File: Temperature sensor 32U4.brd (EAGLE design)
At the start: 66 x 35.6 mm, 30 parts, among them IC1 ATMEGA32U4-AU, IC2 LM2940CS-5.0_NOPB, T1 BD139, X1 16MHz

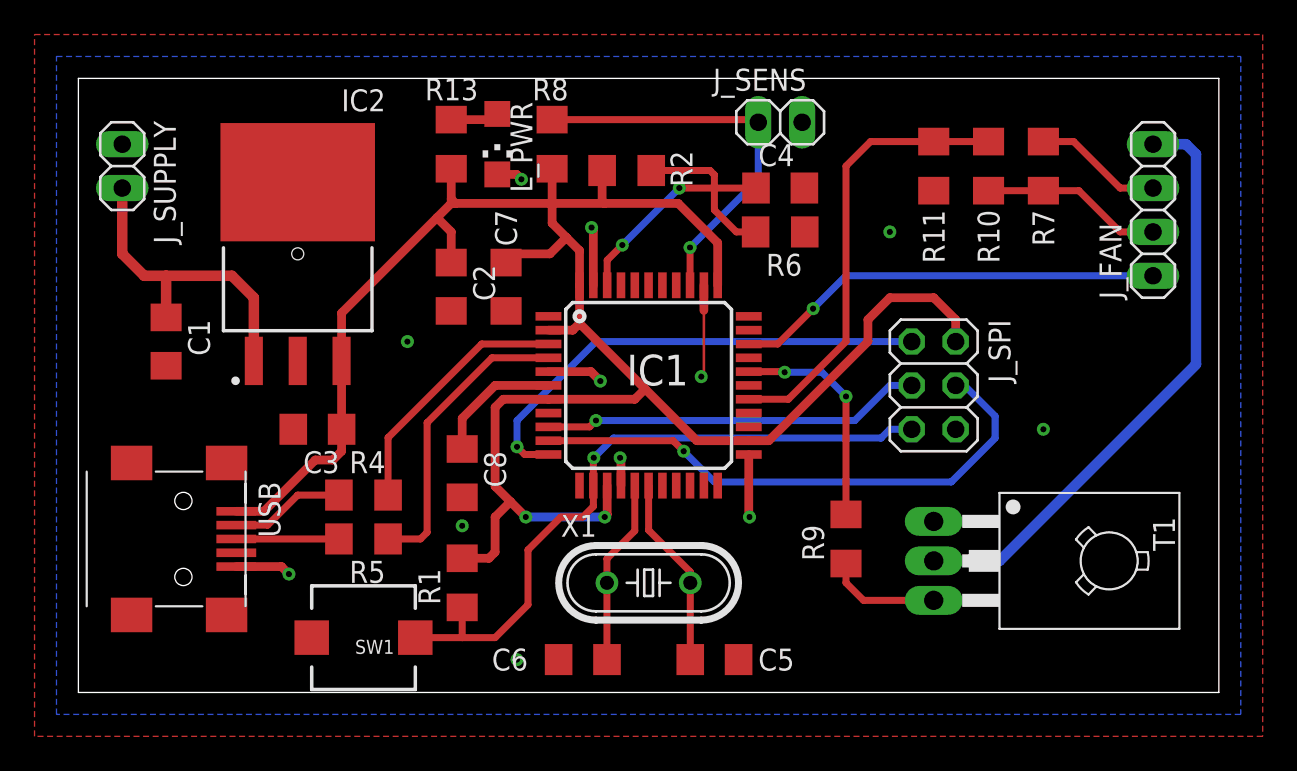
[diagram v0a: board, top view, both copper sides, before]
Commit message: Fixed schematic and deleted backup files
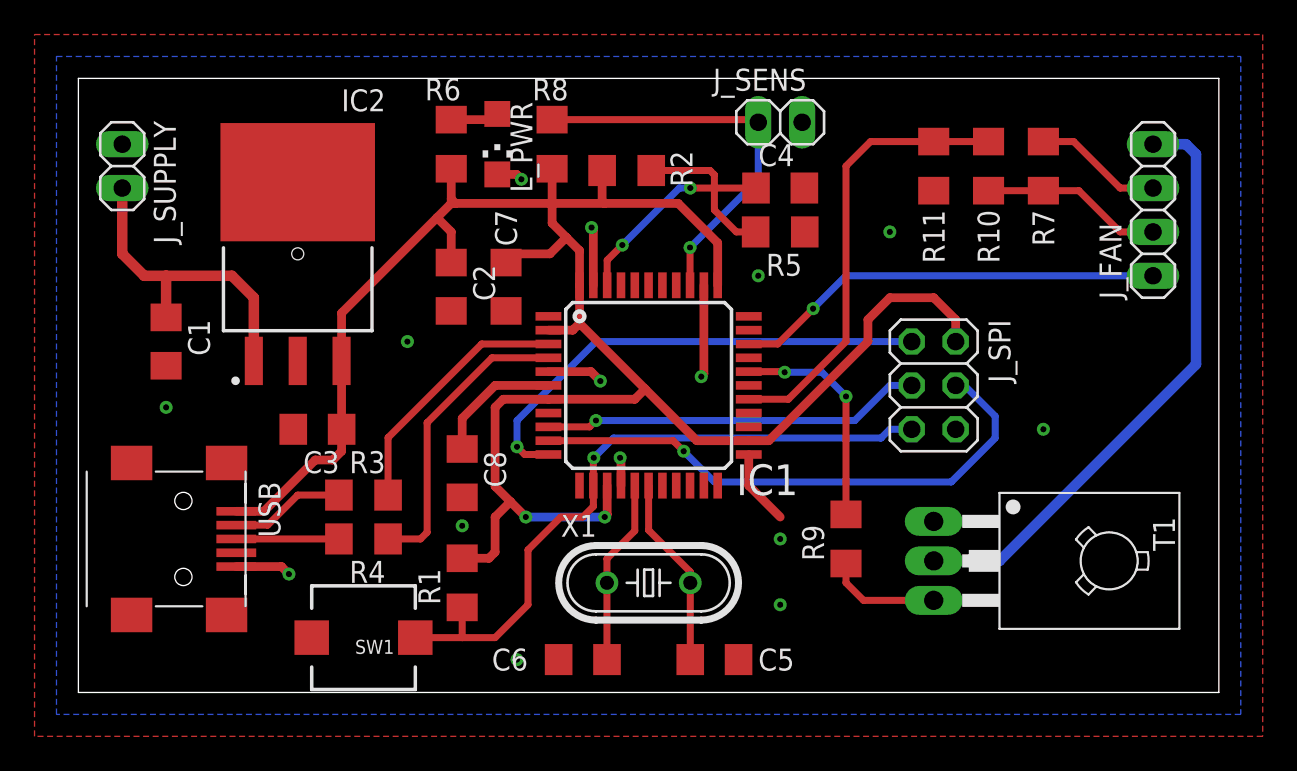
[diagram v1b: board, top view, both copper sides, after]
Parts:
- removed R13: 270, rcl:R1206
- added R3: 10, rcl:R1206
- R5: value 10 -> 8,2k
- R6: value 8,2k -> 270
- moved R5 30.0 mm to (40.6, 26.7)
- moved R6 19.7 mm to (21.6, 31.8), turned to 90 degrees
- moved R4 2.54 mm to (16.5, 8.89)
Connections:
- net +5V: now also R6.1; no longer R13.1
- net AREF: now also R5.2; no longer R6.2
- net D+: now also R4.1; no longer R5.1
- net D-: now also R3.1; no longer R4.1
- net GND: now also R5.1; no longer R6.1
- net N$1: now also R6.2; no longer R13.2
- net USB_D+: now also R4.2; no longer R5.2
- net USB_D-: now also R3.2; no longer R4.2
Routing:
- net GND: track 23.4 -> 22.7 mm, vias 12 -> 15
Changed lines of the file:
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@@
 </element>
 <element name="IC1" library="adafruit" package="TQFP44" value="ATMEGA32U4-AU" x="33.02" y="17.78" smashed="yes">
-<attribute name="NAME" x="31.749996875" y="17.779996875" size="1.778" layer="25"/>
+<attribute name="NAME" x="38.1" y="11.43" size="1.778" layer="25"/>
 </element>
 <element name="IC2" library="LM2940CS-5.0_NOPB" package="TO254P1435X464-4N" value="LM2940CS-5.0_NOPB" x="12.7" y="25.4" smashed="yes" rot="R90">
@@
 <attribute name="SPICEPREFIX" value="R" x="2.54" y="-25.4" size="1.778" layer="27" rot="R270" display="off"/>
 </element>
-<element name="R13" library="rcl" library_urn="urn:adsk.eagle:library:334" package="R1206" package3d_urn="urn:adsk.eagle:package:23540/2" value="270" x="21.59" y="31.75" smashed="yes" rot="R90">
+<element name="R6" library="rcl" library_urn="urn:adsk.eagle:library:334" package="R1206" package3d_urn="urn:adsk.eagle:package:23540/2" value="270" x="21.59" y="31.75" smashed="yes" rot="R90">
 <attribute name="NAME" x="20.066" y="34.29" size="1.27" layer="25"/>
 <attribute name="POPULARITY" value="41" x="74.93" y="46.99" size="1.778" layer="27" rot="R90" display="off"/>
@@
 <attribute name="SPICEPREFIX" value="R" x="2.54" y="70.866" size="1.778" layer="27" rot="R180" display="off"/>
 </element>
-<element name="R4" library="rcl" library_urn="urn:adsk.eagle:library:334" package="R1206" package3d_urn="urn:adsk.eagle:package:23540/2" value="10" x="16.51" y="11.43" smashed="yes" rot="R180">
+<element name="R3" library="rcl" library_urn="urn:adsk.eagle:library:334" package="R1206" package3d_urn="urn:adsk.eagle:package:23540/2" value="10" x="16.51" y="11.43" smashed="yes" rot="R180">
 <attribute name="NAME" x="17.78" y="13.97" size="1.27" layer="25" rot="R180"/>
 <attribute name="POPULARITY" value="41" x="-8.89" y="58.42" size="1.778" layer="27" rot="R180" display="off"/>
 <attribute name="SPICEPREFIX" value="R" x="-8.89" y="58.42" size="1.778" layer="27" rot="R180" display="off"/>
 </element>
-<element name="R5" library="rcl" library_urn="urn:adsk.eagle:library:334" package="R1206" package3d_urn="urn:adsk.eagle:package:23540/2" value="10" x="16.51" y="8.89" smashed="yes" rot="R180">
+<element name="R4" library="rcl" library_urn="urn:adsk.eagle:library:334" package="R1206" package3d_urn="urn:adsk.eagle:package:23540/2" value="10" x="16.51" y="8.89" smashed="yes" rot="R180">
 <attribute name="NAME" x="17.78" y="7.62" size="1.27" layer="25" rot="R180"/>
 <attribute name="POPULARITY" value="41" x="-13.97" y="55.88" size="1.778" layer="27" rot="R180" display="off"/>
 <attribute name="SPICEPREFIX" value="R" x="-13.97" y="55.88" size="1.778" layer="27" rot="R180" display="off"/>
 </element>
-<element name="R6" library="rcl" library_urn="urn:adsk.eagle:library:334" package="R1206" package3d_urn="urn:adsk.eagle:package:23540/2" value="8,2k" x="40.64" y="26.67" smashed="yes" rot="R180">
+<element name="R5" library="rcl" library_urn="urn:adsk.eagle:library:334" package="R1206" package3d_urn="urn:adsk.eagle:package:23540/2" value="8,2k" x="40.64" y="26.67" smashed="yes" rot="R180">
 <attribute name="NAME" x="41.91" y="25.4" size="1.27" layer="25" rot="R180"/>
 <attribute name="POPULARITY" value="41" x="5.08" y="67.31" size="1.778" layer="27" rot="R180" display="off"/>
@@
 <contactref element="J_SPI" pad="6"/>
 <contactref element="USB" pad="GND"/>
-<contactref element="R6" pad="1"/>
+<contactref element="R5" pad="1"/>
 <contactref element="IC1" pad="5"/>
 <contactref element="IC1" pad="15"/>
@@
 <contactref element="IC2" pad="4"/>
 <contactref element="R11" pad="2"/>
-<contactref element="T1" pad="1"/>
 <contactref element="J_SENS" pad="2"/>
 <contactref element="SW1" pad="P$1"/>
@@
 <vertex x="-2.54" y="-2.54"/>
 </polygon>
-<wire x1="36.22" y1="23.58" x2="36.22" y2="22.123" width="0.508" layer="1"/>
 <via x="36.068" y="18.288" extent="1-16" drill="0.35"/>
-<via x="38.862" y="10.16" extent="1-16" drill="0.35"/>
+<via x="40.64" y="8.89" extent="1-16" drill="0.35"/>
 <via x="31.369" y="13.589" extent="1-16" drill="0.35"/>
 <wire x1="31.42" y1="11.98" x2="31.42" y2="13.538" width="0.508" layer="1"/>
 <wire x1="31.42" y1="13.538" x2="31.369" y2="13.589" width="0.508" layer="1"/>
-<wire x1="38.862" y1="10.16" x2="38.82" y2="10.202" width="0.508" layer="1"/>
-<wire x1="38.82" y1="10.202" x2="38.82" y2="13.78" width="0.508" layer="1"/>
+<wire x1="40.639996875" y1="10.160003125" x2="38.82" y2="11.98" width="0.508" layer="1"/>
+<wire x1="38.82" y1="11.98" x2="38.82" y2="13.78" width="0.508" layer="1"/>
 <via x="12.192" y="6.858" extent="1-16" drill="0.35"/>
 <wire x1="9.144" y1="7.29" x2="11.76" y2="7.29" width="0.508" layer="1"/>
@@
 <via x="55.88" y="15.24" extent="1-16" drill="0.35"/>
 <via x="25.4" y="1.905" extent="1-16" drill="0.35"/>
-<wire x1="36.22" y1="23.58" x2="36.22" y2="18.44" width="0.1524" layer="1"/>
-<wire x1="36.22" y1="18.44" x2="36.068" y2="18.288" width="0.1524" layer="1"/>
+<via x="40.64" y="5.08" extent="1-16" drill="0.35"/>
+<via x="39.37" y="24.13" extent="1-16" drill="0.35"/>
+<wire x1="36.22" y1="23.58" x2="36.22" y2="18.44" width="0.508" layer="1"/>
+<wire x1="36.22" y1="18.44" x2="36.068" y2="18.288" width="0.508" layer="1"/>
+<via x="5.08" y="16.51" extent="1-16" drill="0.35"/>
+<contactref element="T1" pad="1"/>
 </signal>
 <signal name="SENS">
@@
 <contactref element="R2" pad="2"/>
 <contactref element="IC1" pad="7"/>
-<contactref element="R13" pad="1"/>
+<contactref element="R6" pad="1"/>
 <contactref element="J_SPI" pad="2"/>
 <contactref element="USB" pad="VBUS"/>
@@
 </signal>
 <signal name="USB_D-">
-<contactref element="R4" pad="2"/>
+<contactref element="R3" pad="2"/>
 <contactref element="USB" pad="D-"/>
 <wire x1="9.144" y1="9.69" x2="10.96" y2="9.69" width="0.4064" layer="1"/>
@@
 </signal>
 <signal name="D-">
-<contactref element="R4" pad="1"/>
+<contactref element="R3" pad="1"/>
 <contactref element="IC1" pad="3"/>
 <wire x1="23.355" y1="20.18" x2="27.22" y2="20.18" width="0.4064" layer="1"/>
@@
 </signal>
 <signal name="USB_D+">
-<contactref element="R5" pad="2"/>
+<contactref element="R4" pad="2"/>
 <contactref element="USB" pad="D+"/>
 <wire x1="9.144" y1="8.89" x2="15.088" y2="8.89" width="0.4064" layer="1"/>
 </signal>
 <signal name="D+">
-<contactref element="R5" pad="1"/>
+<contactref element="R4" pad="1"/>
 <contactref element="IC1" pad="4"/>
 <wire x1="17.932" y1="8.89" x2="19.812" y2="8.89" width="0.4064" layer="1"/>
@@
 <signal name="AREF">
 <contactref element="R2" pad="1"/>
-<contactref element="R6" pad="2"/>
+<contactref element="R5" pad="2"/>
 <contactref element="IC1" pad="42"/>
 <contactref element="C4" pad="1"/>
@@
 <wire x1="36.576" y1="30.226" x2="36.83" y2="29.972" width="0.4064" layer="1"/>
 <wire x1="36.83" y1="29.972" x2="36.83" y2="29.21" width="0.4064" layer="1"/>
-<wire x1="36.83" y1="29.21" x2="34.798" y2="29.21" width="0.4064" layer="1"/>
-<via x="34.798" y="29.21" extent="1-16" drill="0.35"/>
-<wire x1="34.798" y1="29.21" x2="31.496" y2="25.908" width="0.4064" layer="16"/>
+<wire x1="36.83" y1="29.21" x2="35.433" y2="29.21" width="0.4064" layer="1"/>
+<via x="35.433" y="29.21" extent="1-16" drill="0.35"/>
 <via x="31.496" y="25.908" extent="1-16" drill="0.35"/>
 <wire x1="31.496" y1="25.908" x2="30.62" y2="25.032" width="0.4064" layer="1"/>
 <wire x1="30.62" y1="25.032" x2="30.62" y2="23.58" width="0.4064" layer="1"/>
+<wire x1="31.496" y1="25.908" x2="34.798" y2="29.21" width="0.4064" layer="16"/>
+<wire x1="34.798" y1="29.21" x2="35.433" y2="29.21" width="0.4064" layer="16"/>
 </signal>
 <signal name="MOSI">
@@
 </signal>
 <signal name="N$1">
-<contactref element="R13" pad="2"/>
+<contactref element="R6" pad="2"/>
 <contactref element="L_PWR" pad="A"/>
 <wire x1="21.59" y1="33.172" x2="23.929" y2="33.172" width="0.508" layer="1"/>
